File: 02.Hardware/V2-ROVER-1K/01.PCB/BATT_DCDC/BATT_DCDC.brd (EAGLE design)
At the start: 20.6 x 34.7 mm, 44 parts, among them K1 FLEX8, K2 FLEX6, Q1 NVTFS9D6P04M8LTAG, Q2 2N7002PW, Q5 2N7002PW, U1 MCP6071T-E/OT, U3 TPS55330RTET, U7 MCP6071T-E/OT

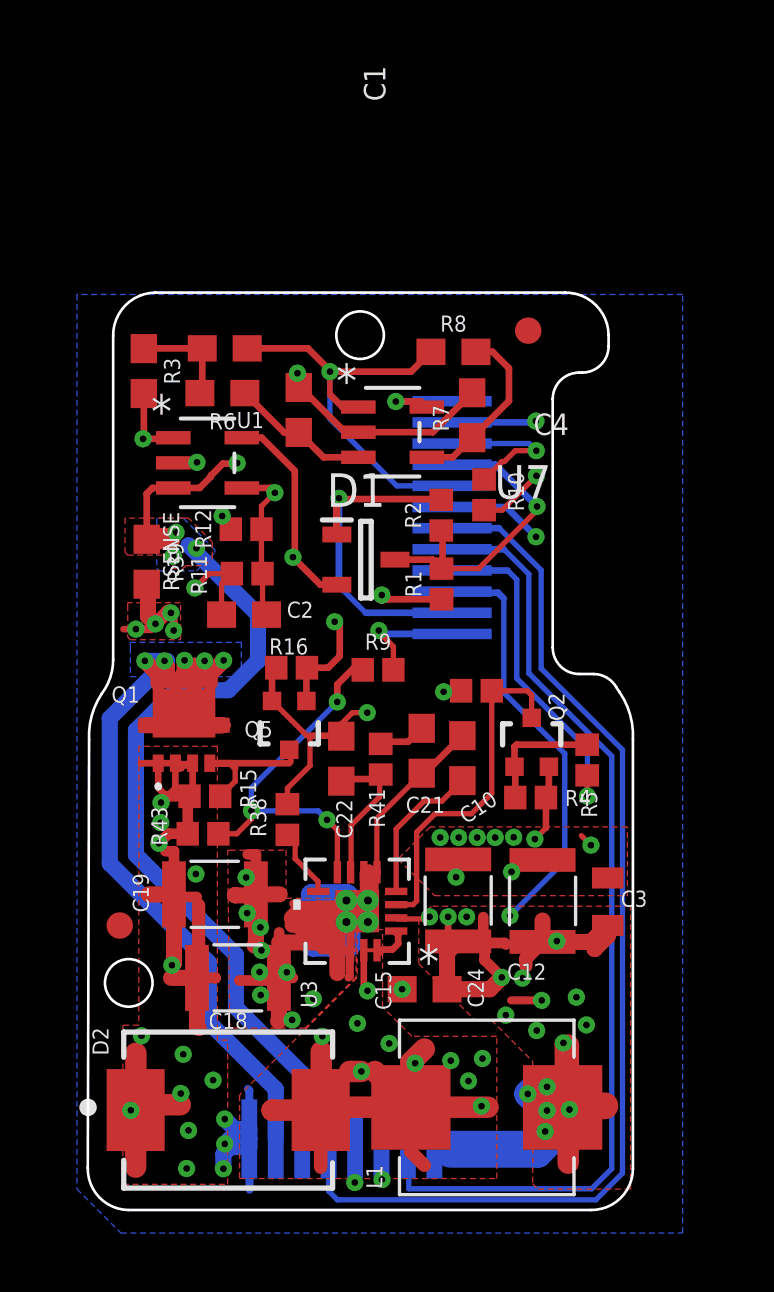
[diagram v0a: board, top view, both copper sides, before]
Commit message: Revision Silk y BOM
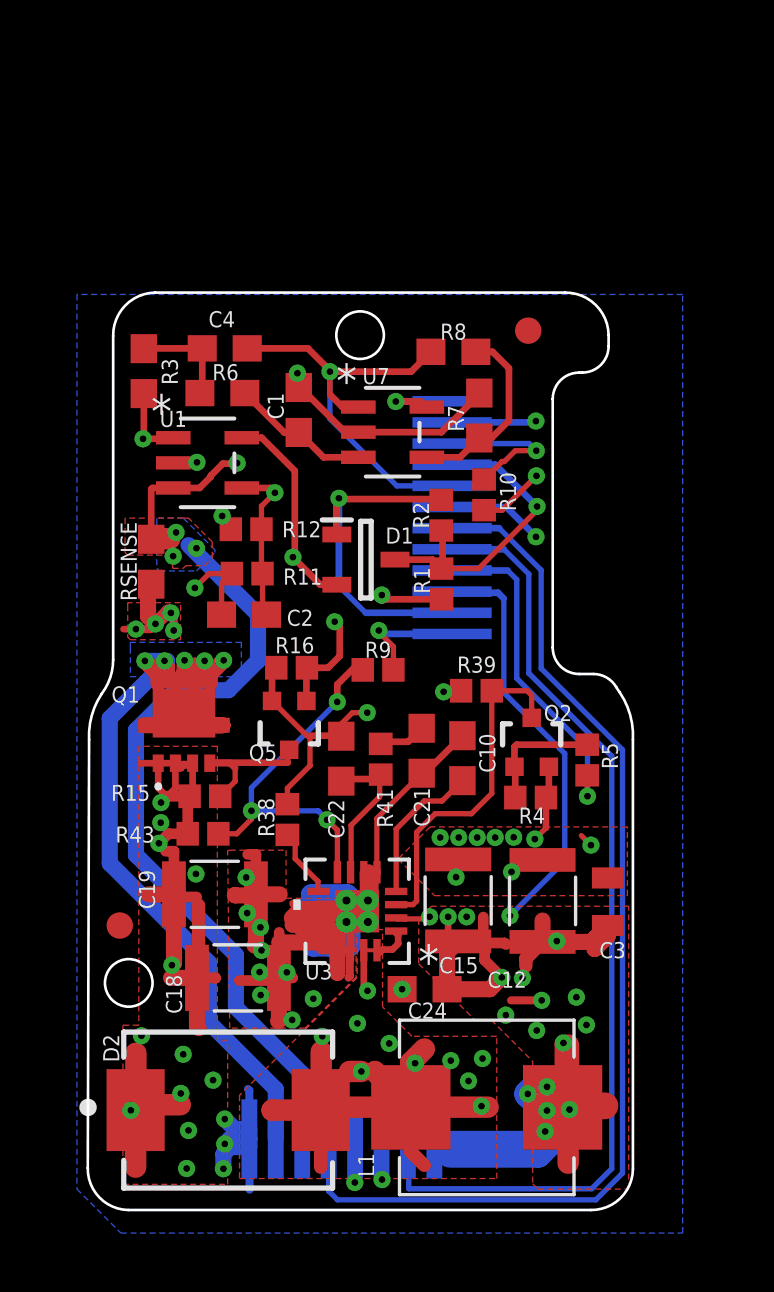
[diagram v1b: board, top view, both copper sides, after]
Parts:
- R10: value 330 -> 330R
- R3, R7: value 2.4k -> 2k4
- R38, R39: value 78.7k -> 78k7
- R43: value 78.7k -> 30k
- R5: value 33 -> 33R
- moved R7 0.27 mm to (72.2, 32.1)
- moved RSENSE 0.17 mm to (59.8, 26.6)

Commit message: Revision 2 - Release candidate (v1)
Se añade resistencia de FB que faltaba (R13)
Se corrige el valor de R9
Se separa la masa de señal (no potencia) de U3 a AGND
Se añaden condensadores de desacoplo para U1 y U7
Corregido el encapsulado de D1 a SOT323
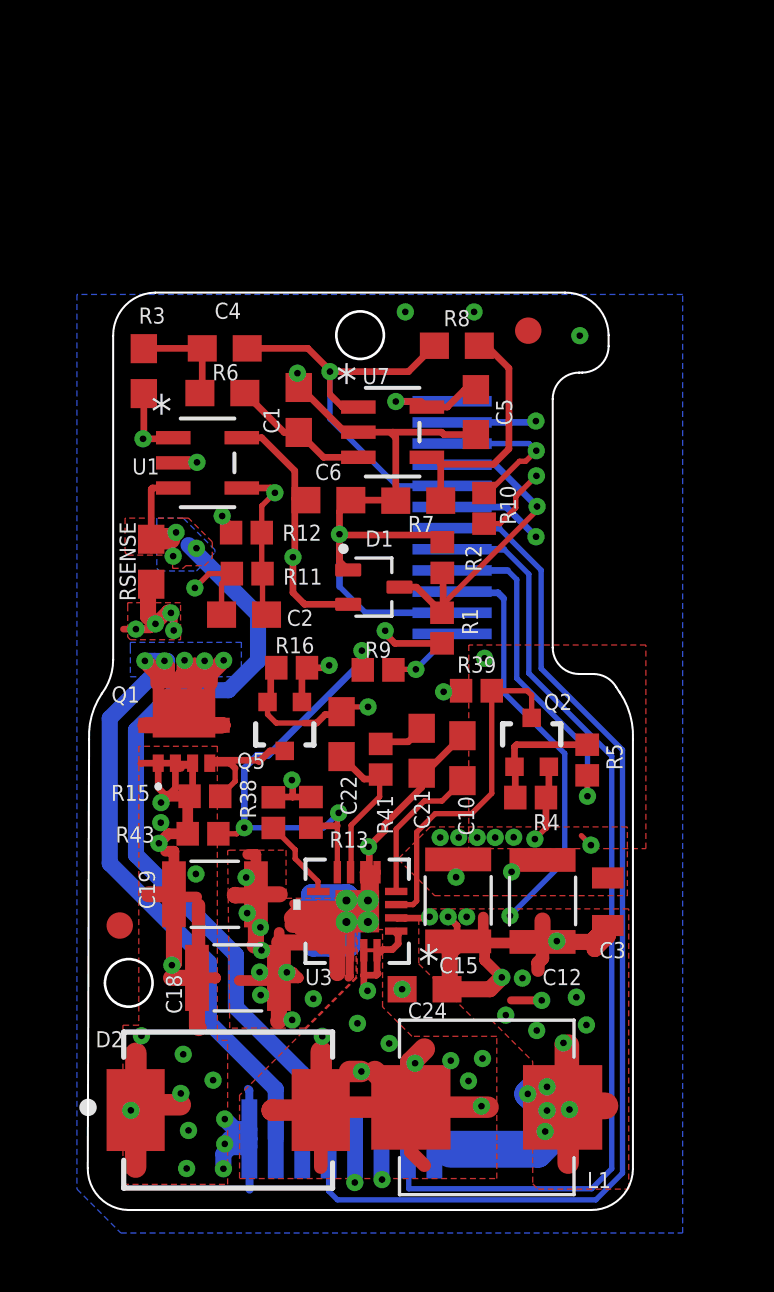
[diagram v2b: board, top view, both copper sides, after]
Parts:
- added C5, C6: 100n, SparkFun-Capacitors:0603
- added R13: 7k5, SparkFun-Resistors:0402
- C2: value 0.1uF -> 100n
- D1: value BAT54S -> BAT54SW,115; device BAT54S:SOT95P240X110-3N -> BAT54SW_115:SOT65P210X110-3N
- R9: value 7k5 -> 5k6
- moved R7 3.96 mm to (69.9, 28.9), turned to 180 degrees
- moved R1 1.67 mm to (70.8, 24.0)
- moved R2 1.60 mm to (70.8, 26.7)
- moved D1 1.08 mm to (68.2, 25.6)
- moved C22 0.93 mm to (67.0, 20.0)
- moved R38 0.59 mm to (64.4, 17.1)
- moved R10 0.51 mm to (72.4, 28.6)
- moved R8 0.26 mm to (71.3, 34.7)
- moved Q5 0.17 mm to (64.8, 20.3)
- moved R12 0.13 mm to (63.4, 27.6)
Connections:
- net FB: now also R13.1
- net GND: now also C5.2, C6.2, R13.2
- net VCC: now also C5.1, C6.1
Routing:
- net GND: track 122.9 -> 130.1 mm, vias 31 -> 37
- net VCC: track 29.7 -> 34.4 mm
- net FB: track 14.3 -> 17.8 mm
- net VOUT-: track 36.6 -> 33.8 mm, vias 4 -> 3
- net N$2: track 7.17 -> 9.36 mm
- net FB_DAC: track 4.54 -> 2.78 mm
- net SW2_TPS: track 26.8 -> 28.3 mm
- net VOUTSENSE: track 12.0 -> 13.0 mm
- added copper zone on layer 15, net N$7
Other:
- board text added: "BATT_DCDC ROVER1K v1-NOV'22"
- board text removed: "BATT_DCDC v5-Jun'21"

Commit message: Cambio de faja por conector interPCB. Issue #1
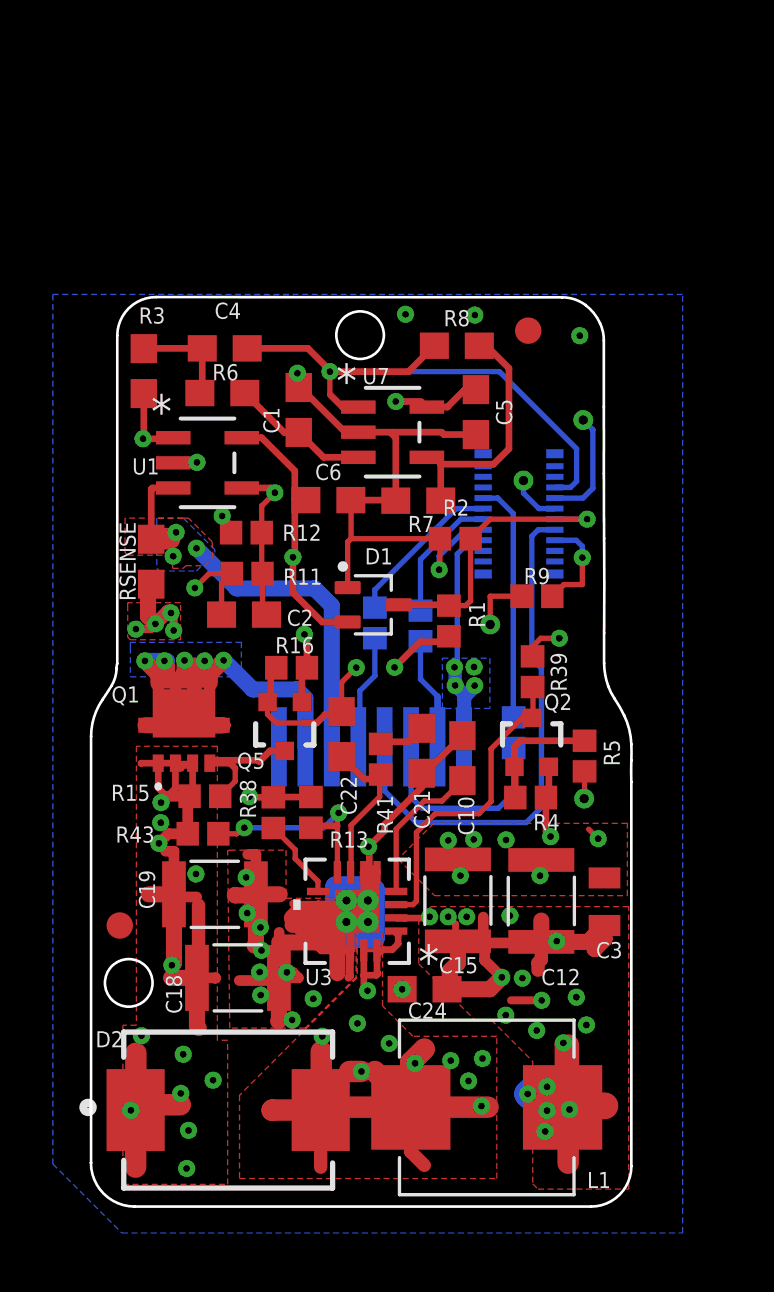
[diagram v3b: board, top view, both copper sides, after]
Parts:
- removed K2: FLEX6, Flex:FLEX6
- added J1: DF40C-20DP-0.4V_51_, DF40C-20DP-0.4V_51_:DF40C-20DPA
- added R14, R17: 100R, SparkFun-Resistors:0402
- moved K1 14.9 mm to (72.4, 17.5)
- moved R10 8.56 mm to (73.5, 20.1), flipped to the bottom
- moved R9 6.62 mm to (74.4, 25.2)
- moved R39 2.24 mm to (74.2, 22.4), turned to 270 degrees
- moved R2 0.86 mm to (71.3, 27.4), turned to 180 degrees
- moved D1 0.67 mm to (68.2, 24.9)
- moved R1 0.37 mm to (71.0, 24.3)
- moved R5 0.18 mm to (76.2, 19.2)
- moved C3 0.12 mm to (76.9, 13.7)
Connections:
- new net N$10: K1.5, R17.2
- new net N$9: K1.2, R14.2
- new net VCC_2: J1.6
- net !RESET: now also J1.8; no longer K2.10
- net EN_DCDC: now also J1.9; no longer K2.4
- net FB_DAC: now also J1.15; no longer K2.1
- net GND: now also J1.14; no longer K2.2
- net IOSENSE: now also J1.5; no longer K2.8
- net OP_SWITCH: now also J1.7; no longer K2.11
- net SWCLK: now also J1.10, R17.1; no longer K1.5, K2.6
- net SWDIO: now also J1.12, R14.1; no longer K1.2, K2.5
- net TXO: now also J1.13; no longer K2.7
- net VBUS: now also J1.16; no longer K2.3
- net VCC: no longer K2.12
- net VOUTSENSE: now also J1.11; no longer K2.9
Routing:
- net SWCLK: track 41.8 -> 6.04 mm
- net N$6: track 41.6 -> 7.90 mm, vias 2 -> 0
- net SWDIO: track 37.0 -> 4.94 mm
- net TXO: track 41.5 -> 19.7 mm, vias 2 -> 0
- net VOUT-: track 33.8 -> 15.9 mm
- net VOUT+: track 51.5 -> 36.9 mm
- net GND: track 130.1 -> 119.7 mm, vias 37 -> 31
- net VCC: track 34.4 -> 39.8 mm
- net IOSENSE: track 17.5 -> 22.8 mm
- net N$10: track 0.00 -> 4.37 mm
- net N$9: track 0.00 -> 4.26 mm
- net EN_DCDC: track 12.7 -> 15.9 mm, vias 1 -> 2
- net !RESET: track 5.93 -> 9.10 mm, vias 1 -> 0
- net FB: track 17.8 -> 20.3 mm
- net OP_SWITCH: track 22.3 -> 24.4 mm
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- added copper zone on layer 16, net VBUS
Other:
- board size 20.6 x 34.7 mm -> 20.4 x 34.4 mm

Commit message: Issue #2
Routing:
- net VOUT+: track 36.9 -> 37.5 mm
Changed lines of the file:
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@@
 <wire x1="61.03" y1="22.8" x2="60.29" y2="22.8" width="0.508" layer="15"/>
 <wire x1="60.29" y1="22.8" x2="59.55" y2="22.8" width="0.508" layer="15"/>
-<wire x1="65.62" y1="19.55" x2="65.62" y2="21.39" width="0.6096" layer="16"/>
-<wire x1="63.63" y1="21.72" x2="62.53" y2="22.82" width="0.6096" layer="16"/>
-<wire x1="65.62" y1="21.39" x2="65.29" y2="21.72" width="0.6096" layer="16"/>
-<wire x1="65.29" y1="21.72" x2="63.63" y2="21.72" width="0.6096" layer="16"/>
+<wire x1="65.62" y1="19.55" x2="65.62" y2="22.33" width="0.6096" layer="16"/>
+<wire x1="62.57" y1="22.78" x2="62.53" y2="22.82" width="0.6096" layer="16"/>
+<wire x1="65.62" y1="22.33" x2="65.17" y2="22.78" width="0.6096" layer="16"/>
+<wire x1="65.17" y1="22.78" x2="62.57" y2="22.78" width="0.6096" layer="16"/>
 <wire x1="62.005" y1="21.965" x2="62.02" y2="21.95" width="0" layer="19" extent="1-1"/>
 <wire x1="62.488" y1="20.365" x2="62.02" y2="20.65" width="0" layer="19" extent="1-1"/>

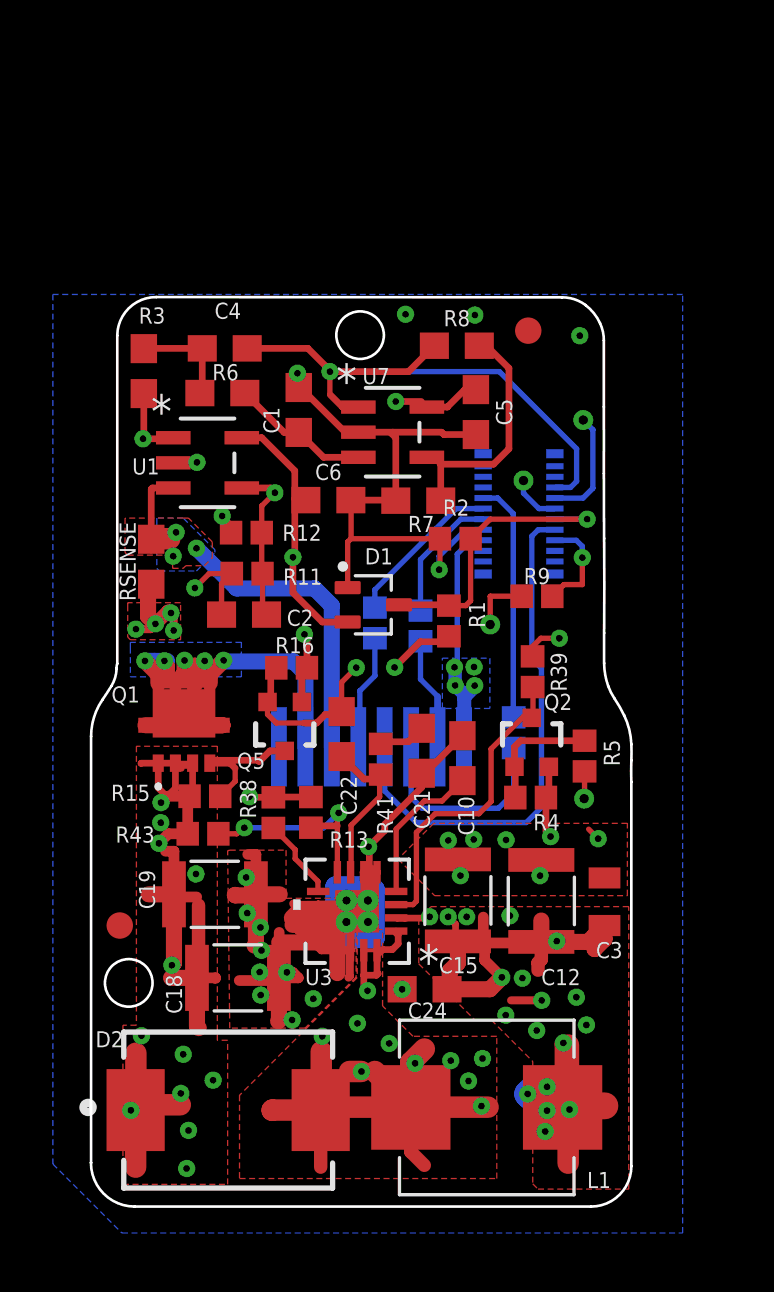
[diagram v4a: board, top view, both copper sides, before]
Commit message: Cambios menores durante revision de proto_1 de SETI
en el esquematico se incluye la frecuencia del FPB del sensado de corriente
en la BRD se aumenta el ancho de la pista de resistencia del DAC
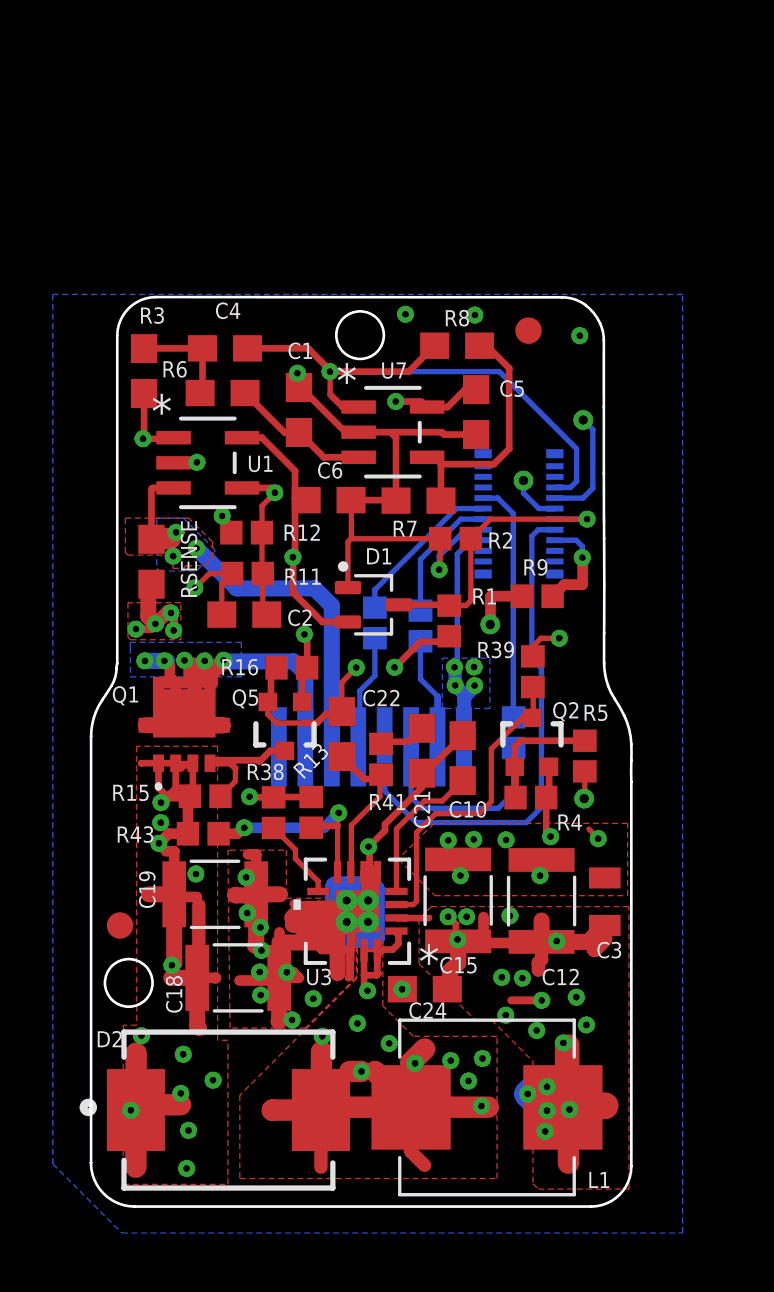
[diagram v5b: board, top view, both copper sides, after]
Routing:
- net VBUS: track 59.6 -> 54.8 mm
- net VOUT+: track 37.5 -> 34.4 mm
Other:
- board text added: "BATT_DCDC ROVER1K v2-DEC'22"
- board text removed: "BATT_DCDC ROVER1K v1-NOV'22"

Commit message: Modificaciones despues de revisar 1er prototipo de SETI
Se van añadiendo modificaciones, pero no están todas las que son necesarias.
Este es el fichero que le paso a Javi para  que comience con el resto de los cambios.
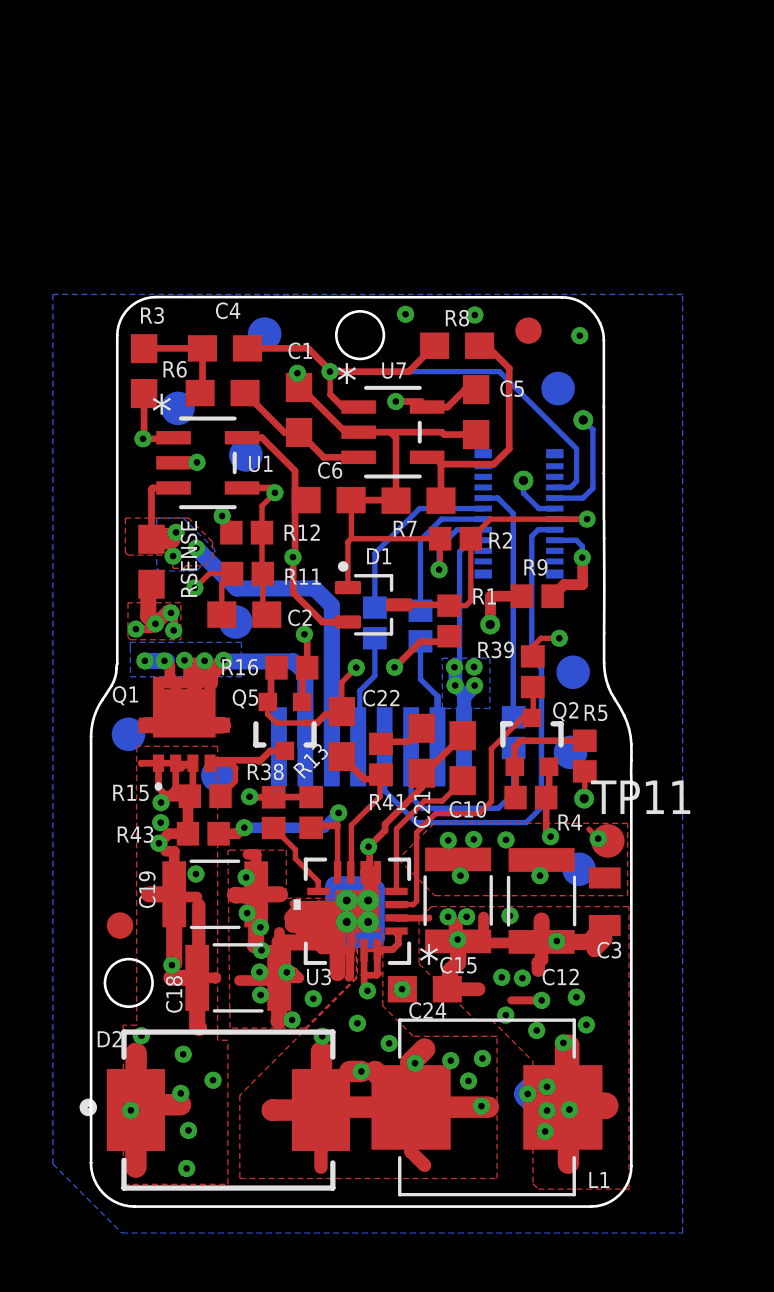
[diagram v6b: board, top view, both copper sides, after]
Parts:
- added TP1, TP10, TP11, TP2, TP3, TP4, TP5, TP6, TP7, TP8, TP9: TESTPAD_TPSQB1,27, BeagleBone_Blue_R3:TESTPAD_B1,27
- C24: value 0.1uF -> 100nF
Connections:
- net EN_DCDC: now also TP6.TP
- net FB_DAC: now also TP2.TP
- net GND: now also TP11.TP, TP3.TP
- net IOSENSE: now also TP5.TP
- net OP_SWITCH: now also TP7.TP
- net VBUS: now also TP1.TP
- net VCC_2: now also TP8.TP
- net VOUT+: now also TP9.TP
- net VOUT-: now also TP10.TP
- net VOUTSENSE: now also TP4.TP
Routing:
- net VBUS: track 54.8 -> 55.9 mm
- net SWCLK: track 6.04 -> 6.85 mm
